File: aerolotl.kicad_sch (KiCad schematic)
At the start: 0 parts

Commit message: added spi
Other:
- sheet External ports: added none; removed SPARE_ADC2
- sheet MCU ports: added AIRBRAKE_PWM1, AIRBRAKE_PWM2, BUZZER_PWM, SPI2{SCK, MISO, MOSI}, SPI4{SCK, MISO, MOSI}; removed SPARE_ADC2
- sheet Power ports: added VOLT_SENSE; removed none

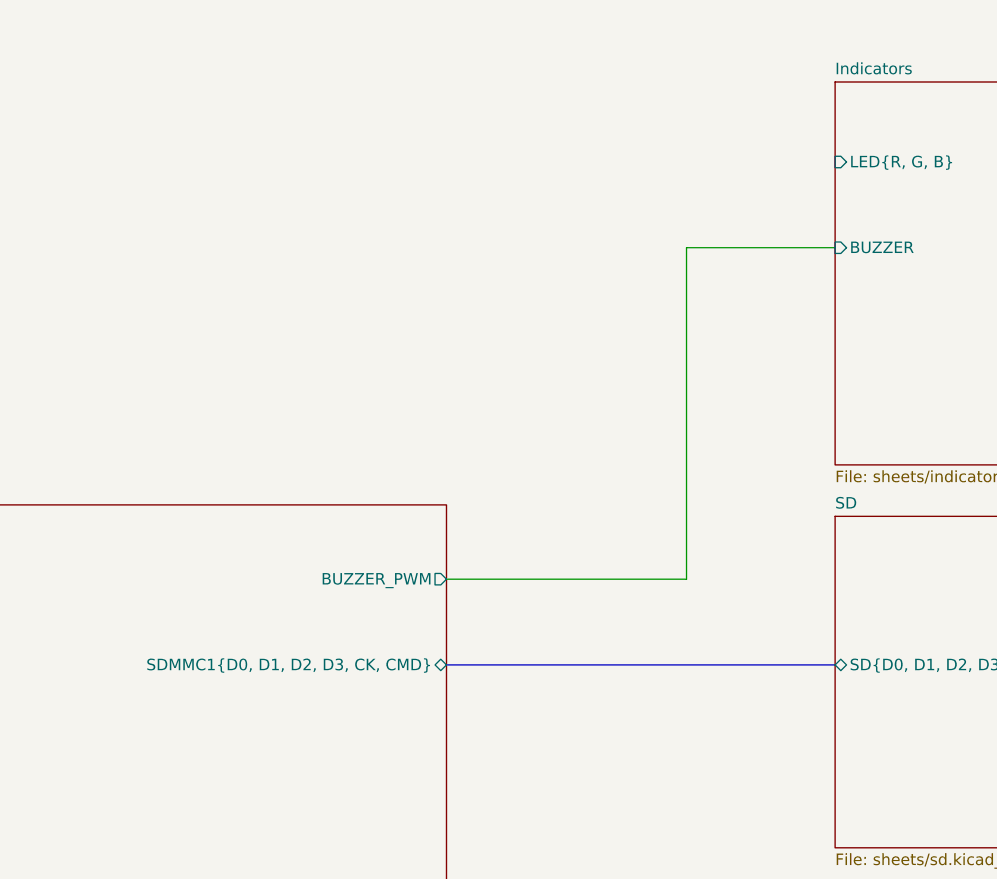
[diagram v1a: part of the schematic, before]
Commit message: led pwm
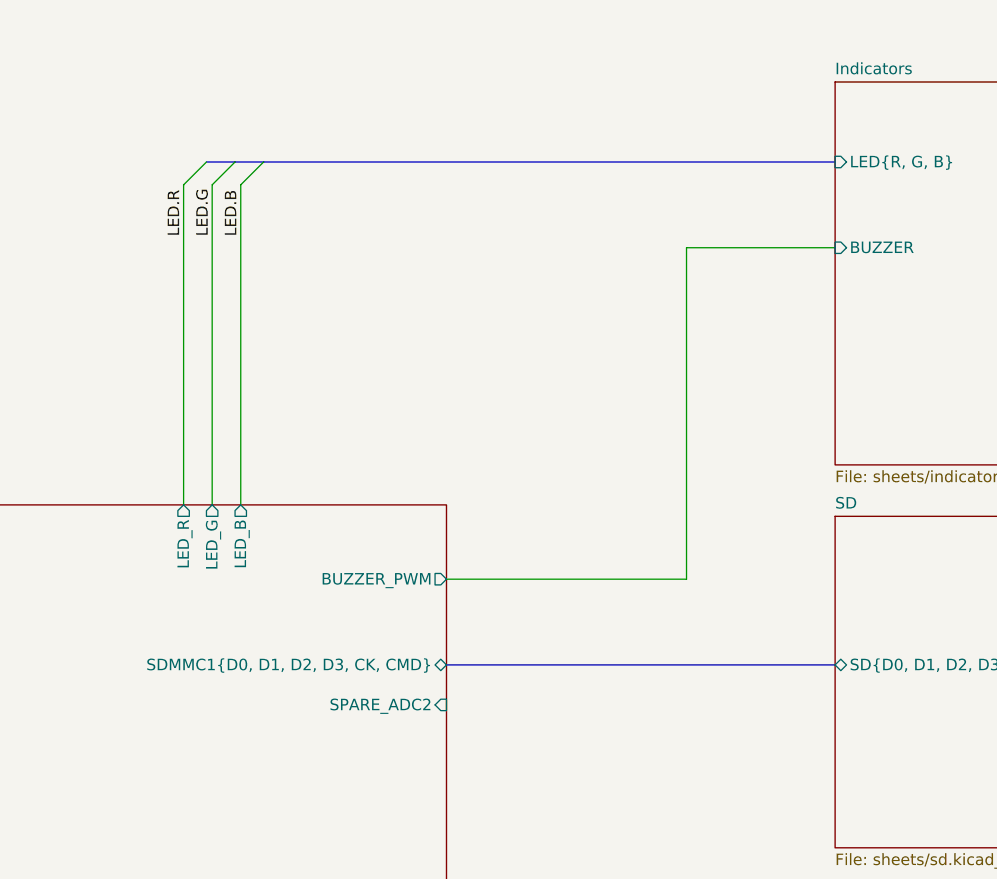
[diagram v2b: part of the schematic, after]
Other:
- sheet MCU ports: added LED_B, LED_G, LED_R, SPARE_ADC2; removed none
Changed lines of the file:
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@@
 	(paper "A3")
+	(bus_entry
+		(at 226.695 46.99)
+		(size -2.54 2.54)
+		(stroke
+			(width 0)
+			(type default)
+		)
+	)
 	(bus_entry
 		(at 204.47 193.675)
@@
 	)
 	(bus_entry
+		(at 229.87 46.99)
+		(size -2.54 2.54)
+		(stroke
+			(width 0)
+			(type default)
+		)
+	)
+	(bus_entry
 		(at 190.5 193.675)
 		(size 2.54 -2.54)
@@
 		)
 	)
+	(bus_entry
+		(at 223.52 46.99)
+		(size -2.54 2.54)
+		(stroke
+			(width 0)
+			(type default)
+		)
+	)
 	(bus
 		(pts
@@
 		)
 	)
+	(bus
+		(pts
+			(xy 223.52 46.99) (xy 226.695 46.99)
+		)
+		(stroke
+			(width 0)
+			(type default)
+		)
+	)
 	(wire
 		(pts
@@
 		)
 	)
+	(wire
+		(pts
+			(xy 227.33 49.53) (xy 227.33 85.09)
+		)
+		(stroke
+			(width 0)
+			(type default)
+		)
+	)
 	(bus
 		(pts
@@
 	(wire
 		(pts
+			(xy 224.155 49.53) (xy 224.155 85.09)
+		)
+		(stroke
+			(width 0)
+			(type default)
+		)
+	)
+	(wire
+		(pts
 			(xy 105.41 52.07) (xy 127 52.07)
 		)
@@
 		)
 	)
+	(bus
+		(pts
+			(xy 229.87 46.99) (xy 293.37 46.99)
+		)
+		(stroke
+			(width 0)
+			(type default)
+		)
+	)
 	(wire
 		(pts
@@
 	(wire
 		(pts
+			(xy 220.98 49.53) (xy 220.98 85.09)
+		)
+		(stroke
+			(width 0)
+			(type default)
+		)
+	)
+	(wire
+		(pts
 			(xy 250.19 170.815) (xy 293.37 170.815)
 		)
@@
 		(pts
 			(xy 200.025 193.675) (xy 204.47 193.675)
+		)
+		(stroke
+			(width 0)
+			(type default)
+		)
+	)
+	(bus
+		(pts
+			(xy 226.695 46.99) (xy 229.87 46.99)
 		)
 		(stroke
@@
 		)
 	)
+	(label "LED.B"
+		(at 227.33 55.245 90)
+		(effects
+			(font
+				(size 1.27 1.27)
+			)
+			(justify left bottom)
+		)
+	)
+	(label "LED.G"
+		(at 224.155 55.245 90)
+		(effects
+			(font
+				(size 1.27 1.27)
+			)
+			(justify left bottom)
+		)
+	)
 	(label "NEOM9N.RST"
 		(at 207.01 191.135 90)
@@
 	(label "NEOM9N.TX"
 		(at 197.485 190.5 90)
+		(effects
+			(font
+				(size 1.27 1.27)
+			)
+			(justify left bottom)
+		)
+	)
+	(label "LED.R"
+		(at 220.98 55.245 90)
 		(effects
 			(font
@@
 			(effects
 				(font
+					(size 1.27 1.27)
+				)
+				(justify right)
+			)
+		)
+		(pin "LED_B" output
+			(at 227.33 85.09 90)
+			(effects
+				(font
+					(size 1.27 1.27)
+				)
+				(justify right)
+			)
+		)
+		(pin "LED_G" output
+			(at 224.155 85.09 90)
+			(effects
+				(font
+					(size 1.27 1.27)
+				)
+				(justify right)
+			)
+		)
+		(pin "LED_R" output
+			(at 220.98 85.09 90)
+			(effects
+				(font
+					(size 1.27 1.27)
+				)
+				(justify right)
+			)
+		)
+		(pin "SPARE_ADC2" input
+			(at 250.19 107.315 0)
+			(effects
+				(font

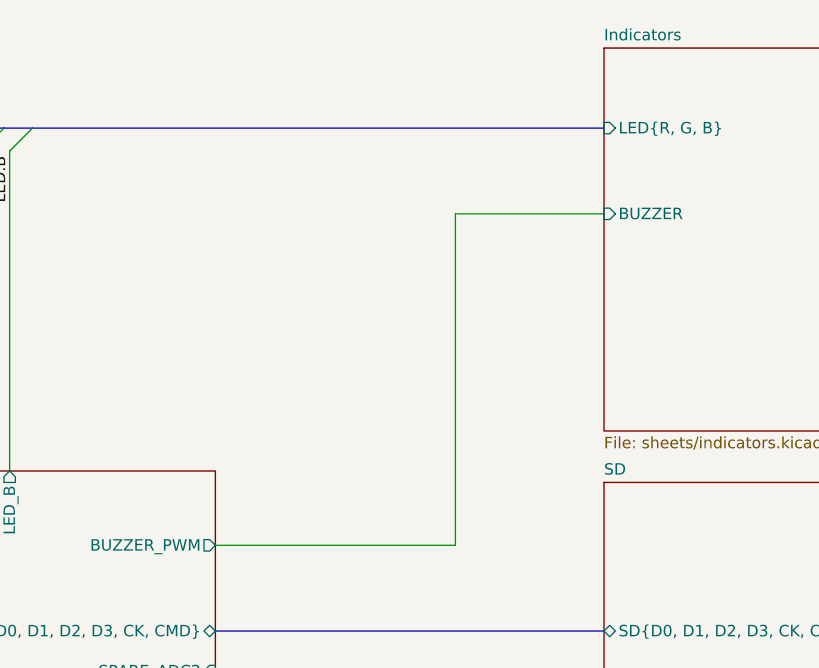
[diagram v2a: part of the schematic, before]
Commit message: assigned gpio pin to led (pg6)
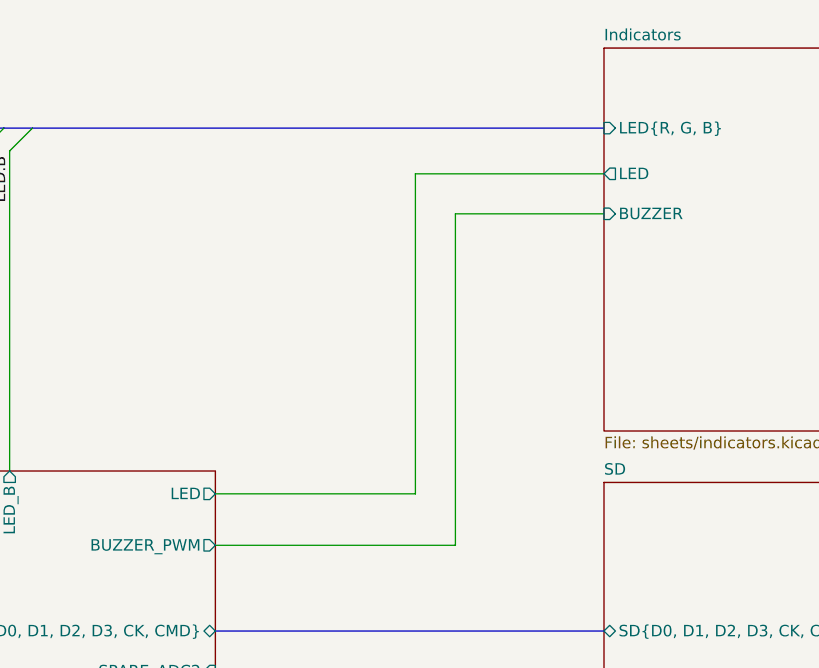
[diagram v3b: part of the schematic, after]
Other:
- sheet Indicators ports: added LED; removed none
- sheet MCU ports: added LED; removed none
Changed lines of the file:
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@@
+		)
+	)
+	(wire
+		(pts
+			(xy 250.19 87.63) (xy 272.415 87.63)
+		)
+		(stroke
+			(width 0)
+			(type default)
 		)
 	)
@@
 		)
 	)
+	(wire
+		(pts
+			(xy 272.415 52.07) (xy 293.37 52.07)
+		)
+		(stroke
+			(width 0)
+			(type default)
+		)
+	)
 	(bus
 		(pts
@@
 		(pts
 			(xy 127 52.07) (xy 127 90.805)
+		)
+		(stroke
+			(width 0)
+			(type default)
+		)
+	)
+	(wire
+		(pts
+			(xy 272.415 87.63) (xy 272.415 52.07)
 		)
 		(stroke
@@
 			)
 		)
+		(pin "LED" output
+			(at 293.37 52.07 180)
+			(effects
+				(font
+					(size 1.27 1.27)
+				)
+				(justify left)
+			)
+		)
 		(instances
 			(project "aerolotl"
@@
 			(effects
 				(font
+					(size 1.27 1.27)
+				)
+				(justify right)
+			)
+		)
+		(pin "LED" output
+			(at 250.19 87.63 0)
+			(effects
+				(font

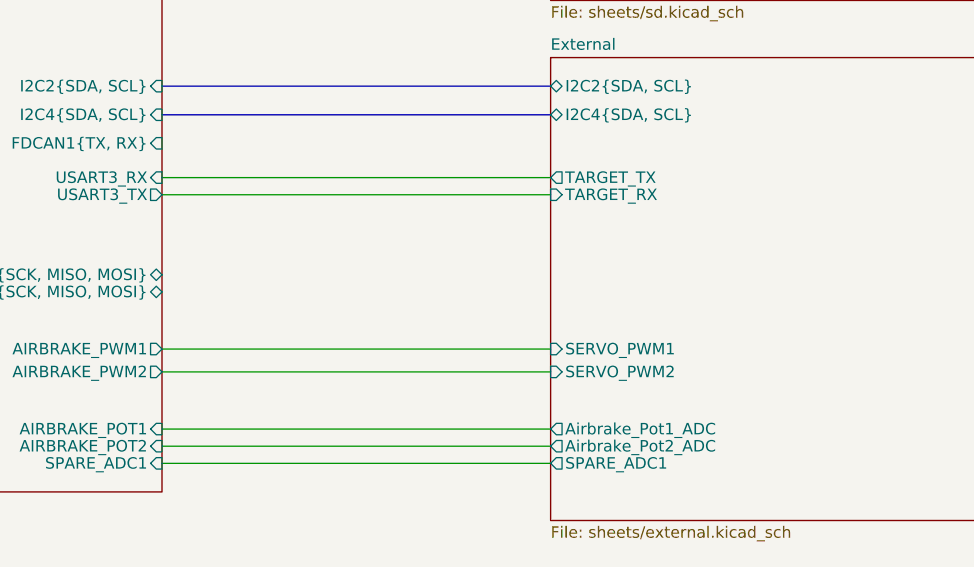
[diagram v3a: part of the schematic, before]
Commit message: assigned gpio pin to led (pg6)
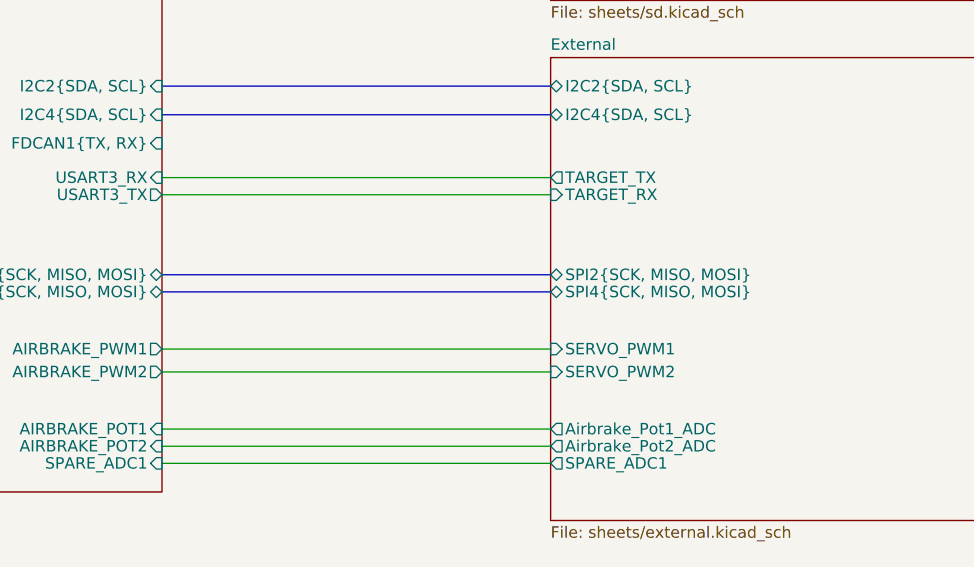
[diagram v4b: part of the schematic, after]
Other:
- sheet External ports: added SPI2{SCK, MISO, MOSI}, SPI4{SCK, MISO, MOSI}; removed none
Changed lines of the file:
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@@
+		)
+	)
+	(bus
+		(pts
+			(xy 250.19 153.67) (xy 293.37 153.67)
+		)
+		(stroke
+			(width 0)
+			(type default)
 		)
 	)
@@
 		(pts
 			(xy 130.81 88.265) (xy 134.62 88.265)
+		)
+		(stroke
+			(width 0)
+			(type default)
+		)
+	)
+	(bus
+		(pts
+			(xy 250.19 155.575) (xy 293.37 155.575)
 		)
 		(stroke
@@
 			(effects
 				(font
+					(size 1.27 1.27)
+				)
+				(justify left)
+			)
+		)
+		(pin "SPI2{SCK, MISO, MOSI}" bidirectional
+			(at 293.37 153.67 180)
+			(effects
+				(font
+					(size 1.27 1.27)
+				)
+				(justify left)
+			)
+		)
+		(pin "SPI4{SCK, MISO, MOSI}" bidirectional
+			(at 293.37 155.575 180)
+			(effects
+				(font

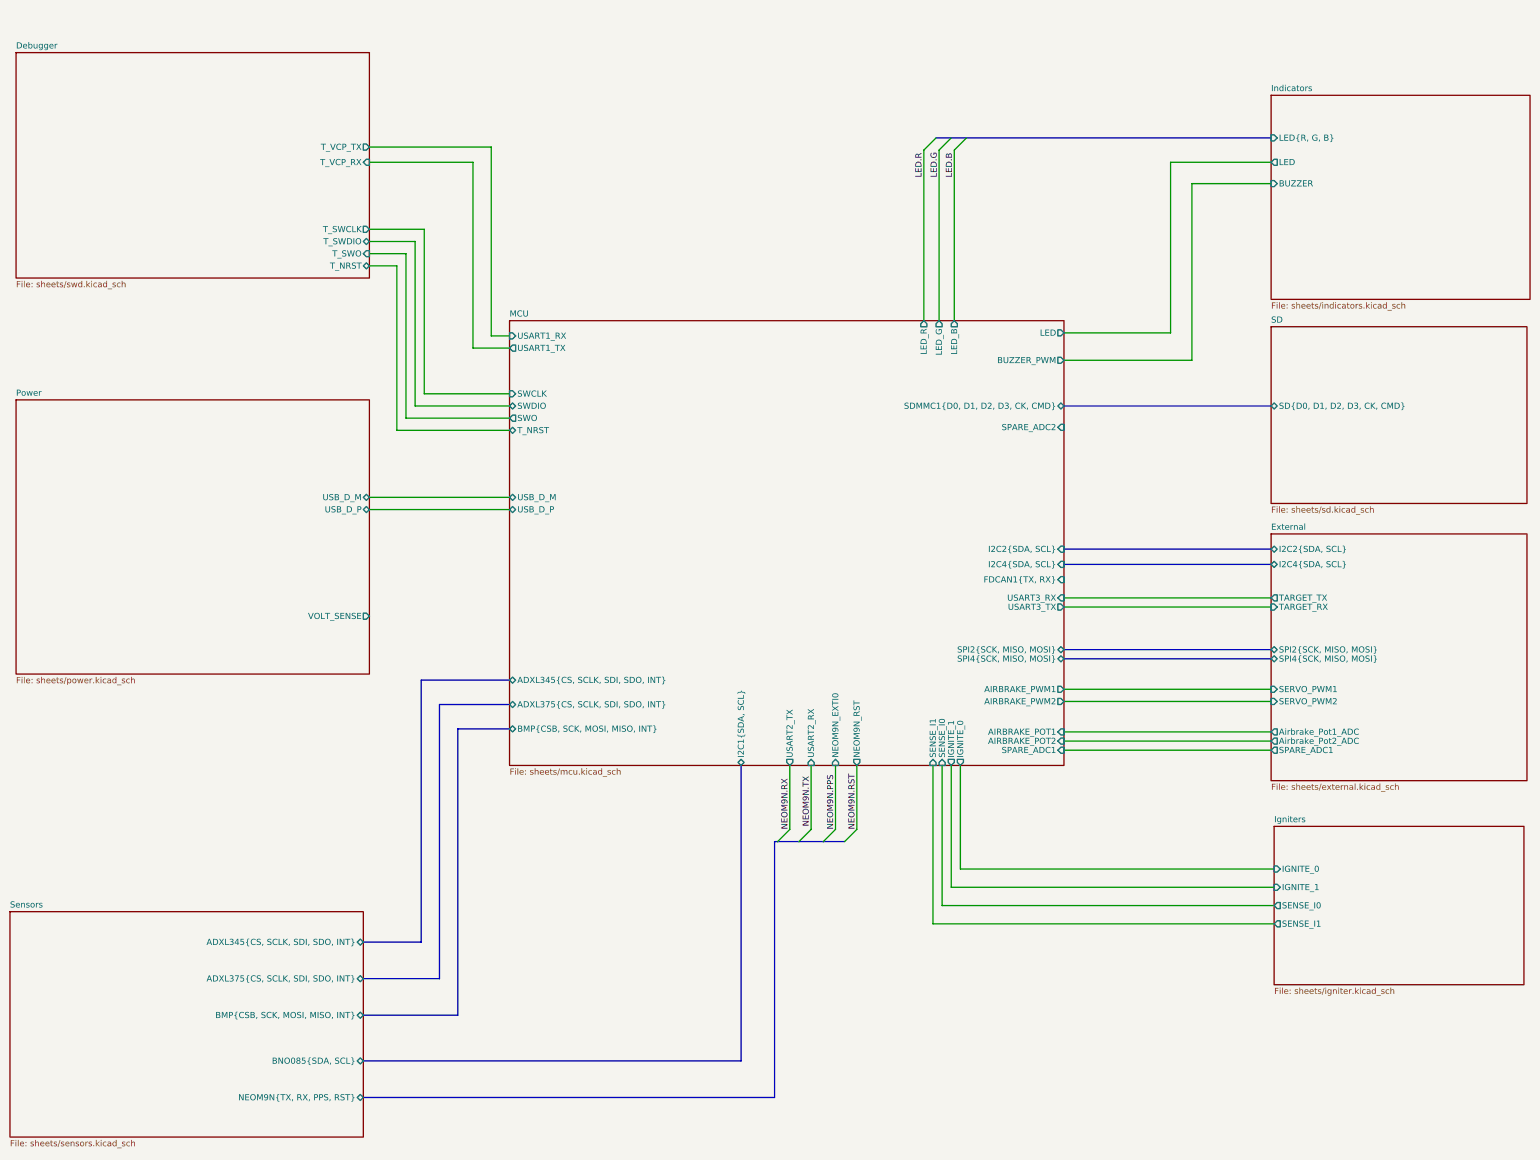
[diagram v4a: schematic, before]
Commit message: added gpio connections in root, UART8, ADC2
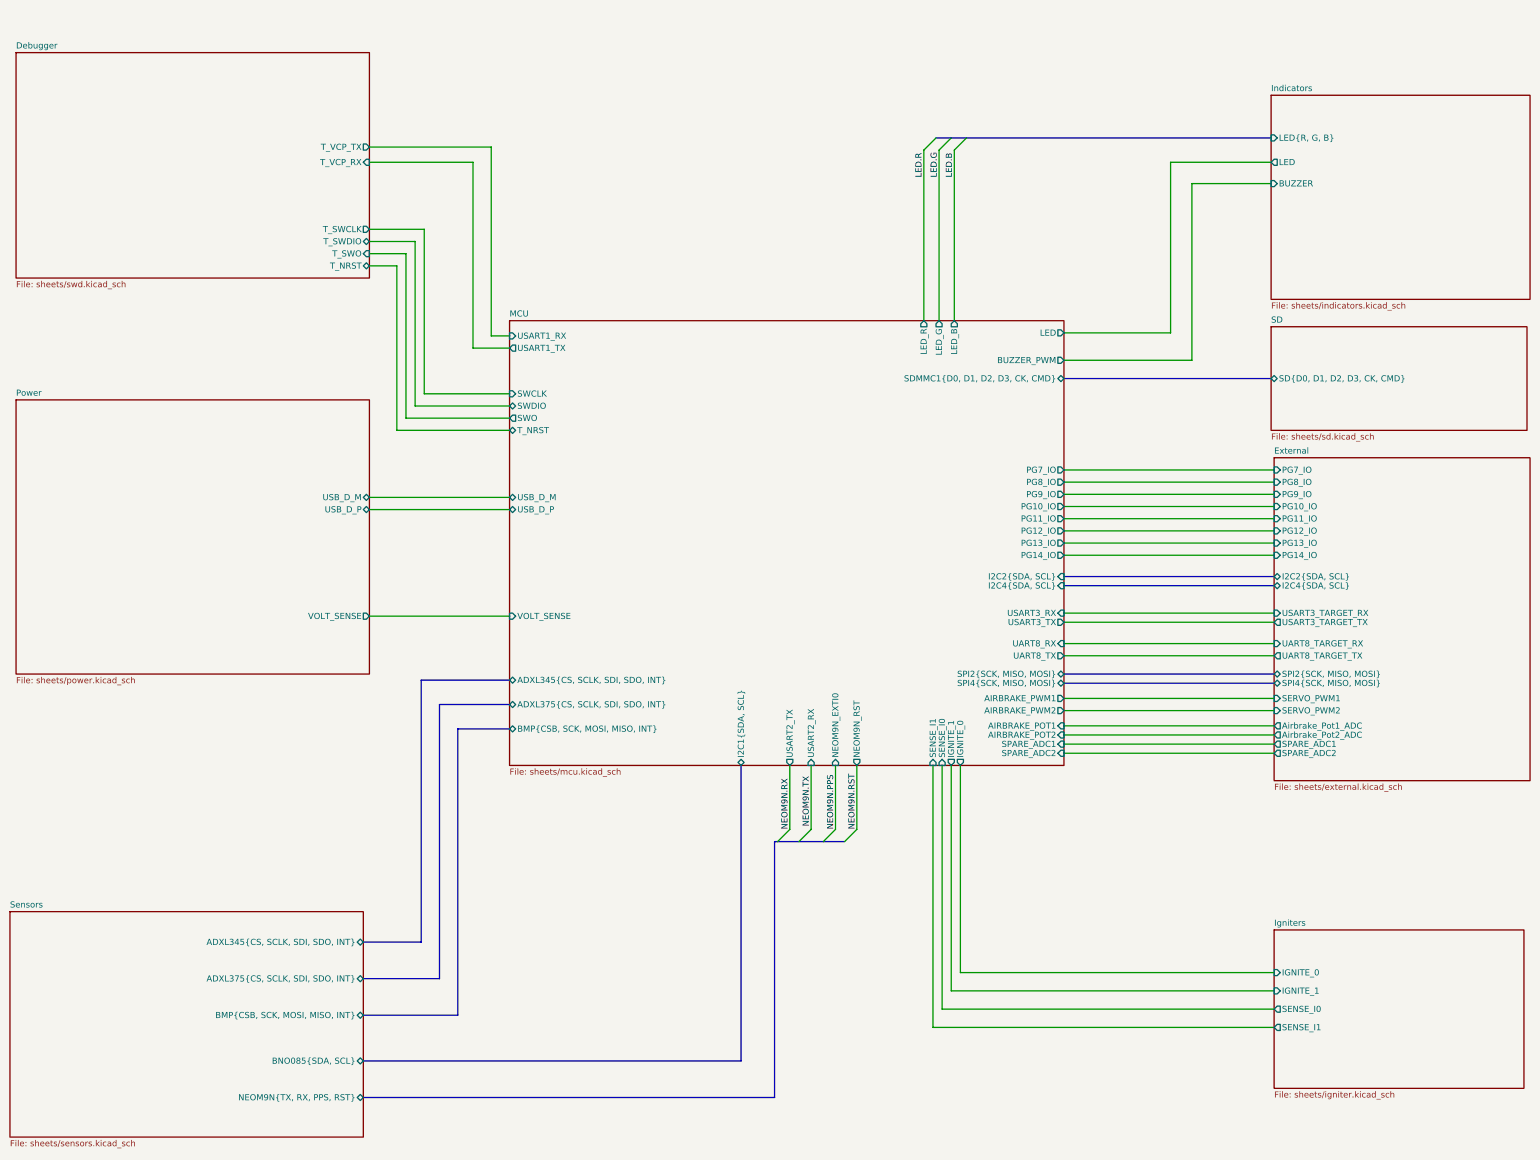
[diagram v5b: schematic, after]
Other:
- sheet External ports: added PG10_IO, PG11_IO, PG12_IO, PG13_IO, PG14_IO, PG7_IO, PG8_IO, PG9_IO, SPARE_ADC2, UART8_TARGET_RX, UART8_TARGET_TX, USART3_TARGET_RX, USART3_TARGET_TX; removed TARGET_RX, TARGET_TX
- sheet MCU ports: added PG10_IO, PG11_IO, PG12_IO, PG13_IO, PG14_IO, PG7_IO, PG8_IO, PG9_IO, UART8_RX, UART8_TX, VOLT_SENSE; removed FDCAN1{TX, RX}
